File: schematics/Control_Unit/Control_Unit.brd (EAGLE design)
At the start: 49.8 x 49.8 mm, 274 parts, among them IC1 74HC174N, IC10 74HC74N, IC101 74HCT08N, IC102 74HC151N, IC103 74HC373N, IC105 74HC151N, IC106 74HC151N, IC108 74HCT32N, IC11 74HC74N, IC110 74HCT32N, IC111 74HC151N, IC112 74HCT32N, IC113 74HC151N, IC114 74HC151N, IC115 74HC151N, IC116 74HC373N, IC117 74HC74N, IC12 74AC08N, IC124 74HCT32N, IC125 74HCT08N, IC126 74AC157N, IC127 74HCT08N, IC128 74AC08N, IC129 74AC08N, IC13 74AC08N, IC134 74HCT08N, IC135 74HCT08N, IC136 74HCT08N, IC14 74HC74N, IC141 74HCT32N, IC15 74HC74N, IC16 74AC08N, IC168 74HCT32N, IC169 74HCT32N, IC17 74HCT32N, IC172 74HCT32N, IC173 74HCT32N, IC175 74HC193N, IC176 74HC193N, IC177 74HC193N, IC178 74HC193N, IC179 74HC193N, IC18 74AC08N, IC180 74HC193N, IC181 74HC193N, IC182 74HC193N, IC19 74AC08N, IC190 74HCT32N, IC191 74HCT32N, IC2 74HC174N, IC20 74AC08N, IC21 74AC08N, IC22 74HCT32N, IC23 74HCT08N, IC24 74HCT08N, IC25 74HCT32N, IC26 74HCT08N, IC27 74HCT08N, IC28 74HCT08N, IC29 74HCT32N, IC3 74HC151N, IC30 74HCT08N, IC31 74HCT00N, IC32 74HCT32N, IC33 74HCT32N, IC34 74HCT08N, IC35 74HCT04N, IC36 74HCT32N, IC37 74ACT02N, IC38 74HCT08N, IC39 74HCT08N, IC4 74HC174N, IC40 74HCT08N, IC41 74HCT08N, IC42 74HC373N, IC43 74HCT04N, IC44 74ACT157N, IC45 74HC373N, IC46 74ACT157N, IC47 74HCT04N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

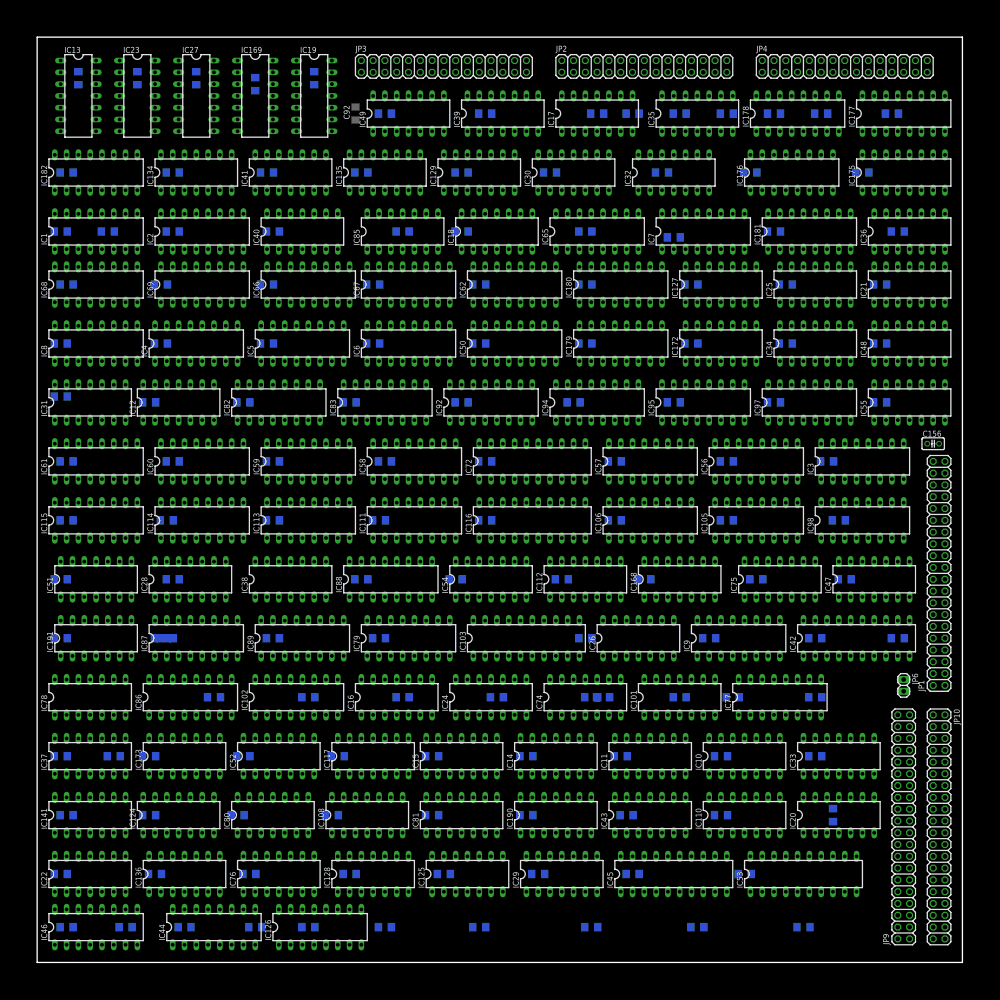
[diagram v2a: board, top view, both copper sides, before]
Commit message: changed register chips to 74xx374
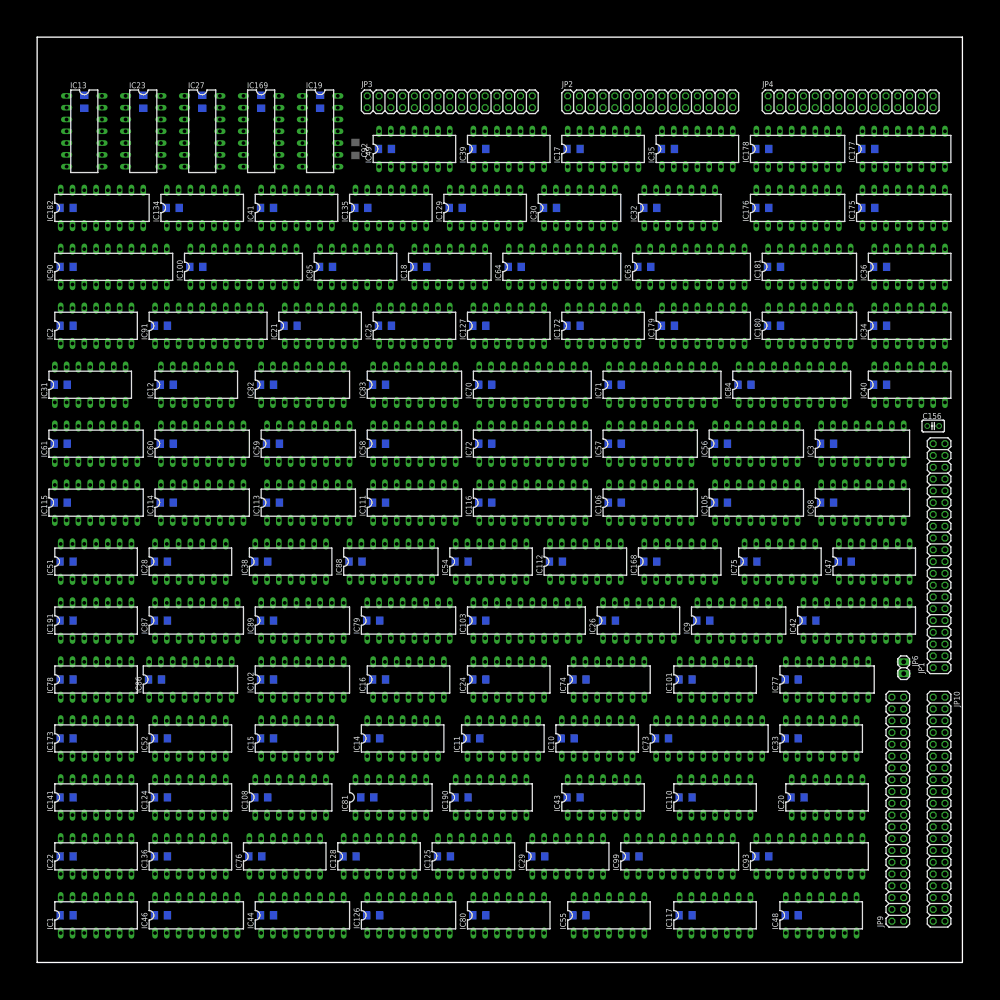
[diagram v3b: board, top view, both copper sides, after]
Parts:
- removed C102, C103, C104, C105, C106, C107, C108, C109, C133, C134, C135, C136, C137, C138, C139, C140, C152, C45, C94, C95, C98: (no value), rcl:C1206
- removed IC37: 74ACT02N, 74xx-eu:DIL14
- removed IC4, IC5, IC50, IC6, IC62, IC65, IC66, IC67, IC68, IC69, IC7, IC8, IC92, IC94, IC95, IC97: 74HC174N, 74xx-eu:DIL16
- removed IC45, IC53: 74HC373N, 74xx-eu:DIL20
- added IC100, IC63, IC64, IC70, IC71, IC73, IC84, IC90, IC91, IC93, IC99: 74HCT374N, 74xx-eu:DIL20
- IC1, IC2: value 74HC174N -> 74HCT32N; device 74xx-eu:DIL16 -> 74xx-eu:DIL14
- moved C90 51.2 mm to (1.59, 8.89)
- moved C22 40.5 mm to (22.9, 8.89), turned to 180 degrees
- moved C121 37.9 mm to (40.6, 2.54)
- moved IC1 36.8 mm to (3.17, 2.54)
- moved C132 34.9 mm to (36.8, 27.9)
- moved C13 34.5 mm to (12.1, 21.6)
- moved IC40 33.7 mm to (47.0, 31.1)
- moved C48 32.2 mm to (28.9, 8.89), turned to 180 degrees
- moved IC55 32.0 mm to (30.8, 2.54)
- moved IC21 31.8 mm to (15.2, 34.3)
- moved C44 31.7 mm to (33.0, 40.6)
- moved IC48 31.2 mm to (42.2, 2.54)
- moved C114 27.1 mm to (33.7, 12.1)
- moved C77 26.8 mm to (13.7, 34.3)
- moved C67 24.9 mm to (23.8, 18.4)
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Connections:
- net !REGISTER_RESET: no longer IC1.1, IC2.1, IC2.11, IC2.13, IC2.14, IC2.6, IC4.1, IC5.1, IC5.11, IC5.13, IC5.14, IC5.6, IC50.1, IC50.11, IC50.13, IC50.14, IC50.6, IC6.1, IC62.1, IC65.1, IC65.11, IC65.13, IC65.14, IC65.6, IC66.1, IC67.1, IC67.11, IC67.13, IC67.14, IC67.6, IC68.1, IC69.1, IC69.11, IC69.13, IC69.14, IC69.6, IC7.1, IC8.1, IC8.11, IC8.13, IC8.14, IC8.6, IC92.1, IC94.1, IC94.11, IC94.13, IC94.14, IC94.6, IC95.1, IC97.1, IC97.11, IC97.13, IC97.14, IC97.6
- net DATA0: now also IC100.3, IC63.3, IC64.3, IC70.3, IC71.3, IC73.3, IC84.3, IC90.3, IC91.3, IC93.3, IC99.3; no longer IC1.3, IC4.3, IC45.3, IC53.3, IC6.3, IC62.3, IC66.3, IC68.3, IC7.3, IC92.3, IC95.3
- net DATA1: now also IC100.4, IC63.4, IC64.4, IC70.4, IC71.4, IC73.4, IC84.4, IC90.4, IC91.4, IC93.4, IC99.4; no longer IC1.4, IC4.4, IC45.4, IC53.4, IC6.4, IC62.4, IC66.4, IC68.4, IC7.4, IC92.4, IC95.4
- net DATA2: now also IC100.7, IC63.7, IC64.7, IC70.7, IC71.7, IC73.7, IC84.7, IC90.7, IC91.7, IC93.7, IC99.7; no longer IC1.6, IC4.6, IC45.7, IC53.7, IC6.6, IC62.6, IC66.6, IC68.6, IC7.6, IC92.6, IC95.6
- net DATA3: now also IC100.8, IC63.8, IC64.8, IC70.8, IC71.8, IC73.8, IC84.8, IC90.8, IC91.8, IC93.8, IC99.8; no longer IC1.11, IC4.11, IC45.8, IC53.8, IC6.11, IC62.11, IC66.11, IC68.11, IC7.11, IC92.11, IC95.11
- net DATA4: now also IC100.13, IC63.13, IC64.13, IC70.13, IC71.13, IC73.13, IC84.13, IC90.13, IC91.13, IC93.13, IC99.13; no longer IC1.13, IC4.13, IC45.13, IC53.13, IC6.13, IC62.13, IC66.13, IC68.13, IC7.13, IC92.13, IC95.13
- net DATA5: now also IC100.14, IC63.14, IC70.14, IC71.14, IC73.14, IC84.14, IC90.14, IC91.14, IC93.14, IC99.14; no longer IC1.14, IC4.14, IC45.14, IC6.14, IC62.14, IC66.14, IC68.14, IC7.14, IC92.14, IC95.14
- net DATA6: now also IC100.17, IC63.17, IC64.14, IC64.17, IC70.17, IC71.17, IC73.17, IC84.17, IC90.17, IC91.17, IC93.17, IC99.17; no longer IC2.3, IC45.17, IC5.3, IC50.3, IC53.14, IC53.17, IC65.3, IC67.3, IC69.3, IC8.3, IC94.3, IC97.3
- net DATA7: now also IC100.18, IC63.18, IC64.18, IC70.18, IC71.18, IC73.18, IC84.18, IC90.18, IC91.18, IC93.18, IC99.18; no longer IC2.4, IC45.18, IC5.4, IC50.4, IC53.18, IC65.4, IC67.4, IC69.4, IC8.4, IC94.4, IC97.4
- net FILL_LR_H_SAVE_LR: now also IC2.12; no longer IC37.11
- net FILL_LR_L_SAVE_LR: now also IC1.4; no longer IC37.5
- net FILL_PTR_H_SET_PTR: now also IC2.5; no longer IC37.3
- net FILL_PTR_L_SET_PTR: now also IC2.2; no longer IC37.9
- net GND: now also IC1.7, IC100.1, IC100.10, IC2.7, IC63.1, IC63.10, IC64.1, IC64.10, IC70.1, IC70.10, IC71.1, IC71.10, IC73.1, IC73.10, IC84.1, IC84.10, IC90.1, IC90.10, IC91.1, IC91.10, IC93.1, IC93.10, IC99.1, IC99.10; no longer C102.2, C103.2, C104.2, C105.2, C106.2, C107.2, C108.2, C109.2, C133.2, C134.2, C135.2, C136.2, C137.2, C138.2, C139.2, C140.2, C152.2, C45.2, C94.2, C95.2, C98.2, IC1.8, IC2.8, IC37.7, IC4.8, IC45.1, IC45.10, IC5.8, IC50.8, IC53.1, IC53.10, IC6.8, IC62.8, IC65.8, IC66.8, IC67.8, IC68.8, IC69.8, IC7.8, IC8.8, IC92.8, IC94.8, IC95.8, IC97.8
- net IO_OUTPUT1_0: now also IC63.2; no longer IC45.2
- net IO_OUTPUT1_1: now also IC63.5; no longer IC45.5
- net IO_OUTPUT1_2: now also IC63.6; no longer IC45.6
- net IO_OUTPUT1_3: now also IC63.9; no longer IC45.9
- net IO_OUTPUT1_4: now also IC63.12; no longer IC45.12
- net IO_OUTPUT1_5: now also IC63.15; no longer IC45.15
- net IO_OUTPUT1_6: now also IC63.16; no longer IC45.16
- net IO_OUTPUT1_7: now also IC63.19; no longer IC45.19
- net IO_OUTPUT2_0: now also IC64.2; no longer IC53.2
- net IO_OUTPUT2_1: now also IC64.5; no longer IC53.5
- net IO_OUTPUT2_2: now also IC64.6; no longer IC53.6
- net IO_OUTPUT2_3: now also IC64.9; no longer IC53.9
- net IO_OUTPUT2_4: now also IC64.12; no longer IC53.12
- net IO_OUTPUT2_5: now also IC64.15; no longer IC53.15
- net IO_OUTPUT2_6: now also IC64.16; no longer IC53.16
- net IO_OUTPUT2_7: now also IC64.19; no longer IC53.19
- net IO_OUTPUT_REG_1_LOAD_INPUT: now also IC63.11; no longer IC45.11
- net IO_OUTPUT_REG_2_LOAD_INPUT: now also IC64.11; no longer IC53.11
- net IR_DATA_OUT_0: now also IC90.2; no longer IC4.2
- net IR_DATA_OUT_1: now also IC90.5; no longer IC4.5
- net IR_DATA_OUT_2: now also IC90.6; no longer IC4.7
- net IR_DATA_OUT_3: now also IC90.9; no longer IC4.10
- net IR_DATA_OUT_4: now also IC90.12; no longer IC4.12
- net IR_DATA_OUT_5: now also IC90.15; no longer IC4.15
- net IR_DATA_OUT_6: now also IC90.16; no longer IC5.2
- net IR_DATA_OUT_7: now also IC90.19; no longer IC5.5
- net IR_LOAD_INPUT: now also IC90.11; no longer IC4.9, IC5.9
- net LR_DATA_OUT_0: now also IC99.2; no longer IC92.2
- net LR_DATA_OUT_1: now also IC99.5; no longer IC92.5
- net LR_DATA_OUT_10: now also IC100.6; no longer IC95.7
- net LR_DATA_OUT_11: now also IC100.9; no longer IC95.10
- net LR_DATA_OUT_12: now also IC100.12; no longer IC95.12
- net LR_DATA_OUT_13: now also IC100.15; no longer IC95.15
- net LR_DATA_OUT_14: now also IC100.16; no longer IC97.2
- net LR_DATA_OUT_15: now also IC100.19; no longer IC97.5
- net LR_DATA_OUT_2: now also IC99.6; no longer IC92.7
- net LR_DATA_OUT_3: now also IC99.9; no longer IC92.10
- net LR_DATA_OUT_4: now also IC99.12; no longer IC92.12
- net LR_DATA_OUT_5: now also IC99.15; no longer IC92.15
- net LR_DATA_OUT_6: now also IC99.16; no longer IC94.2
- net LR_DATA_OUT_7: now also IC99.19; no longer IC94.5
- net LR_DATA_OUT_8: now also IC100.2; no longer IC95.2
- net LR_DATA_OUT_9: now also IC100.5; no longer IC95.5
- net LR_H_LOAD_INPUT_NOT: now also IC100.11, IC2.11; no longer IC37.13, IC95.9, IC97.9
- net LR_H_LOAD_INPUT_TABLE_1: now also IC2.13; no longer IC37.12
- net LR_L_LOAD_INPUT_NOT: now also IC1.6, IC99.11; no longer IC37.4, IC92.9, IC94.9
- net LR_L_LOAD_INPUT_TABLE_1: now also IC1.5; no longer IC37.6
- net OPCODE_0: now also IC91.2; no longer IC6.2
- net OPCODE_1: now also IC91.5; no longer IC6.5
- net OPCODE_2: now also IC91.6; no longer IC6.7
- net OPCODE_3: now also IC91.9; no longer IC6.10
- net OPCODE_4: now also IC91.12; no longer IC6.12
- net OPCODE_5: now also IC91.15; no longer IC6.15
- net OPCODE_6: now also IC91.16; no longer IC50.2
- net OPCODE_7: now also IC91.19; no longer IC50.5
- net OPCODE_LOAD_INPUT/CYCL_2: now also IC91.11; no longer IC50.9, IC6.9
- net PC_COUNT_UP: now also IC2.8; no longer IC54.4
- net PC_COUNT_UP_FETCH1: now also IC2.9; no longer IC54.5
- net PC_COUNT_UP_FETCH2/CYCL_5: now also IC2.10; no longer IC54.6
- net PTR_DATA_OUT_0: now also IC93.2; no longer IC1.2
- net PTR_DATA_OUT_1: now also IC93.5; no longer IC1.5
- net PTR_DATA_OUT_2: now also IC93.6; no longer IC1.7
- net PTR_DATA_OUT_3: now also IC93.9; no longer IC1.10
- net PTR_DATA_OUT_4: now also IC93.12; no longer IC1.12
- net PTR_DATA_OUT_5: now also IC93.15; no longer IC1.15
- net PTR_DATA_OUT_6: now also IC93.16; no longer IC2.2
- net PTR_DATA_OUT_7: now also IC93.19; no longer IC2.5
- net PTR_H_LOAD_INPUT_NOT: now also IC2.6; no longer IC37.1
- net PTR_L_LOAD_INPUT_NOT: now also IC2.3, IC93.11; no longer IC1.9, IC2.9, IC37.10
- net REG_0_LOAD_INPUT: now also IC84.11; no longer IC7.9, IC8.9
- net REG_0_OUT_0: now also IC84.2; no longer IC7.2
- net REG_0_OUT_1: now also IC84.5; no longer IC7.5
- net REG_0_OUT_2: now also IC84.6; no longer IC7.7
- net REG_0_OUT_3: now also IC84.9; no longer IC7.10
- net REG_0_OUT_4: now also IC84.12; no longer IC7.12
- net REG_0_OUT_5: now also IC84.15; no longer IC7.15
- net REG_0_OUT_6: now also IC84.16; no longer IC8.2
- net REG_0_OUT_7: now also IC84.19; no longer IC8.5
- net REG_1_LOAD_INPUT: now also IC70.11; no longer IC62.9, IC65.9
- net REG_1_OUT_0: now also IC70.2; no longer IC62.2
- net REG_1_OUT_1: now also IC70.5; no longer IC62.5
- net REG_1_OUT_2: now also IC70.6; no longer IC62.7
- net REG_1_OUT_3: now also IC70.9; no longer IC62.10
- net REG_1_OUT_4: now also IC70.12; no longer IC62.12
- net REG_1_OUT_5: now also IC70.15; no longer IC62.15
- net REG_1_OUT_6: now also IC70.16; no longer IC65.2
- net REG_1_OUT_7: now also IC70.19; no longer IC65.5
- net REG_2_LOAD_INPUT: now also IC73.11; no longer IC66.9, IC67.9
- net REG_2_OUT_0: now also IC73.2; no longer IC66.2
- net REG_2_OUT_1: now also IC73.5; no longer IC66.5
- net REG_2_OUT_2: now also IC73.6; no longer IC66.7
- net REG_2_OUT_3: now also IC73.9; no longer IC66.10
- net REG_2_OUT_4: now also IC73.12; no longer IC66.12
- net REG_2_OUT_5: now also IC73.15; no longer IC66.15
- net REG_2_OUT_6: now also IC73.16; no longer IC67.2
- net REG_2_OUT_7: now also IC73.19; no longer IC67.5
- net REG_3_LOAD_INPUT: now also IC71.11; no longer IC68.9, IC69.9
- net REG_3_OUT_0: now also IC71.2; no longer IC68.2
- net REG_3_OUT_1: now also IC71.5; no longer IC68.5
- net REG_3_OUT_2: now also IC71.6; no longer IC68.7
- net REG_3_OUT_3: now also IC71.9; no longer IC68.10
- net REG_3_OUT_4: now also IC71.12; no longer IC68.12
- net REG_3_OUT_5: now also IC71.15; no longer IC68.15
- net REG_3_OUT_6: now also IC71.16; no longer IC69.2
- net REG_3_OUT_7: now also IC71.19; no longer IC69.5
- net TABLE_1_INPUT_PTR_HIGH: now also IC2.4; no longer IC37.2
- net TABLE_1_INPUT_PTR_L: now also IC2.1; no longer IC37.8
- net VCC: now also IC1.14, IC100.20, IC2.14, IC63.20, IC64.20, IC70.20, IC71.20, IC73.20, IC84.20, IC90.20, IC91.20, IC93.20, IC99.20; no longer C102.1, C103.1, C104.1, C105.1, C106.1, C107.1, C108.1, C109.1, C133.1, C134.1, C135.1, C136.1, C137.1, C138.1, C139.1, C140.1, C152.1, C45.1, C94.1, C95.1, C98.1, IC1.16, IC2.16, IC37.14, IC4.16, IC45.20, IC5.16, IC50.16, IC53.20, IC6.16, IC62.16, IC65.16, IC66.16, IC67.16, IC68.16, IC69.16, IC7.16, IC8.16, IC92.16, IC94.16, IC95.16, IC97.16

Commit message: forgot it
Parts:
- removed C156: (no value), rcl:C025-025X050
- moved IC79 17.5 mm to (37.5, 18.4)
- moved IC101 16.8 mm to (20.0, 18.4)
- moved IC103 15.6 mm to (41.6, 15.2)
- moved C67 11.7 mm to (35.6, 18.4)
- moved IC77 7.30 mm to (35.2, 15.2)
- moved C35 6.67 mm to (24.1, 18.4)
- moved C61 6.67 mm to (29.2, 18.4)
- moved IC26 6.67 mm to (25.7, 18.4)
- moved IC9 6.35 mm to (31.4, 18.4)
- moved C150 1.59 mm to (33.3, 15.2)
- moved C122 1.27 mm to (8.89, 47.6)
- moved C18 1.27 mm to (44.8, 45.1)
- moved C23 1.27 mm to (28.9, 45.1)
- moved C26 1.27 mm to (39.1, 45.1)
- moved C49 1.27 mm to (2.54, 47.6)
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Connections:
- net ADRR_15: now also IC17.9; no longer IC25.9
- net FILL_PC_H_RET: now also IC1.1; no longer IC17.12
- net FILL_PC_L_JMP_O: now also IC1.12; no longer IC80.9
- net FILL_PC_L_RET: now also IC1.13; no longer IC80.10
- net GND: no longer C156.2
- net MEM_NOT_CE: now also IC17.10, IC17.13; no longer IC25.10, IC36.2
- net N$12: now also IC49.13; no longer IC49.12
- net N$163: now also IC1.11; no longer IC80.8
- net N$171: now also IC36.6; no longer IC17.8
- net N$31: now also IC17.11; no longer IC36.3
- net N$32: now also IC1.8; no longer IC36.6
- net N$33: now also IC1.3; no longer IC17.11
- net N$67: now also IC17.12; no longer IC36.1
- net N$70: now also IC17.8; no longer IC25.8
- net PC_H_LOAD_INPUT_TABLE_1: now also IC1.2; no longer IC17.13
- net PC_LOW_LOAD_INPUT_JMP: now also IC1.9; no longer IC36.4
- net PC_L_LOAD_INPUT_TABLE_1: now also IC1.10; no longer IC36.5
- net VCC: now also IC49.12; no longer C156.1, IC49.13
- net WRITE_LR_H_DBUS_RET: now also IC36.4; no longer IC17.9
- net WRITE_PC_L_DBUS_SAVE_LR: now also IC36.5; no longer IC17.10

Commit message: regroup
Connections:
- net CONNECT_PTR_TO_ABUS/CLR_NOT_OE_LDR: now also IC36.1; no longer IC25.4
- net CONNECT_PTR_TO_ABUS/CONNECT_REG_TO_DBUS/CLR_NOT_WE/SELECTOR_TABLE_2_STR: now also IC36.2; no longer IC25.5
- net N$190: now also IC80.10; no longer IC25.2
- net N$192: now also IC80.9; no longer IC25.1
- net N$193: now also IC80.8; no longer IC25.3
- net PTR_TO_ABUS/!PC_TO_ABUS: now also IC36.3; no longer IC25.6

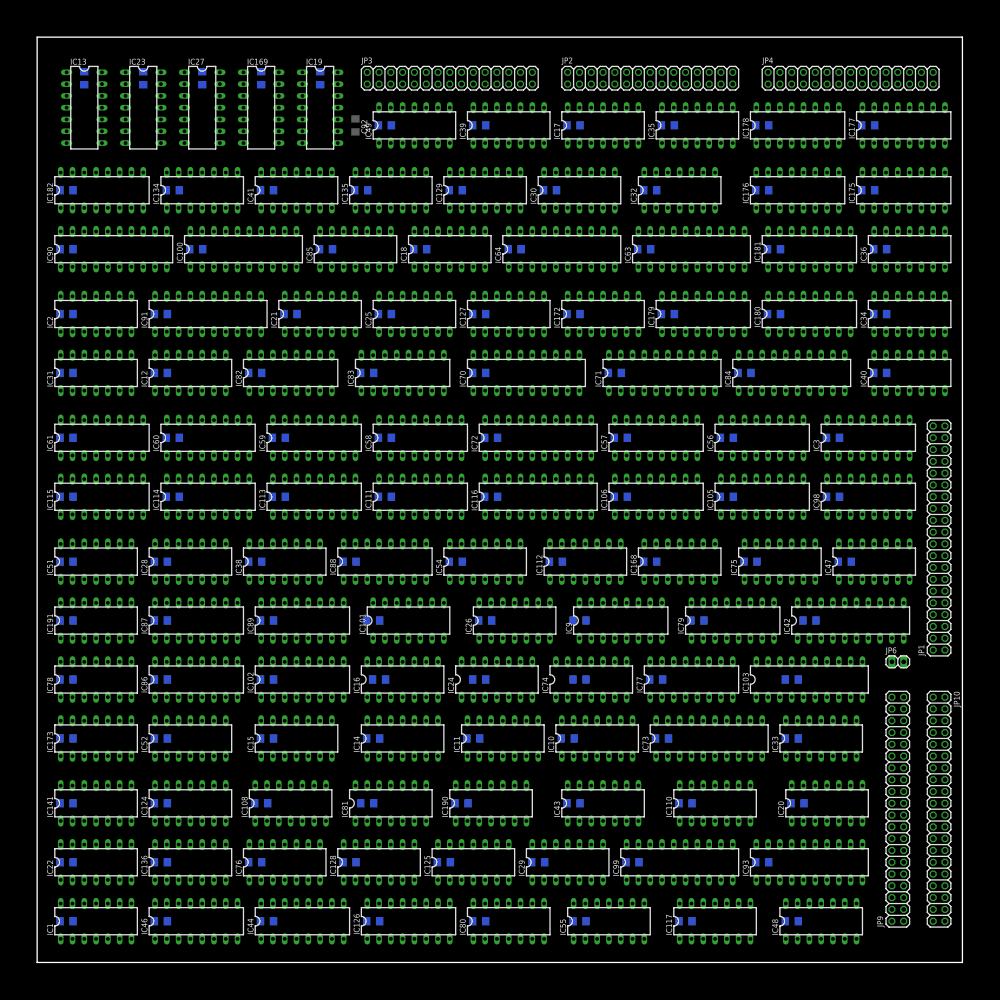
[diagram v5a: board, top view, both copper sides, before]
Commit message: optimize chip count :)
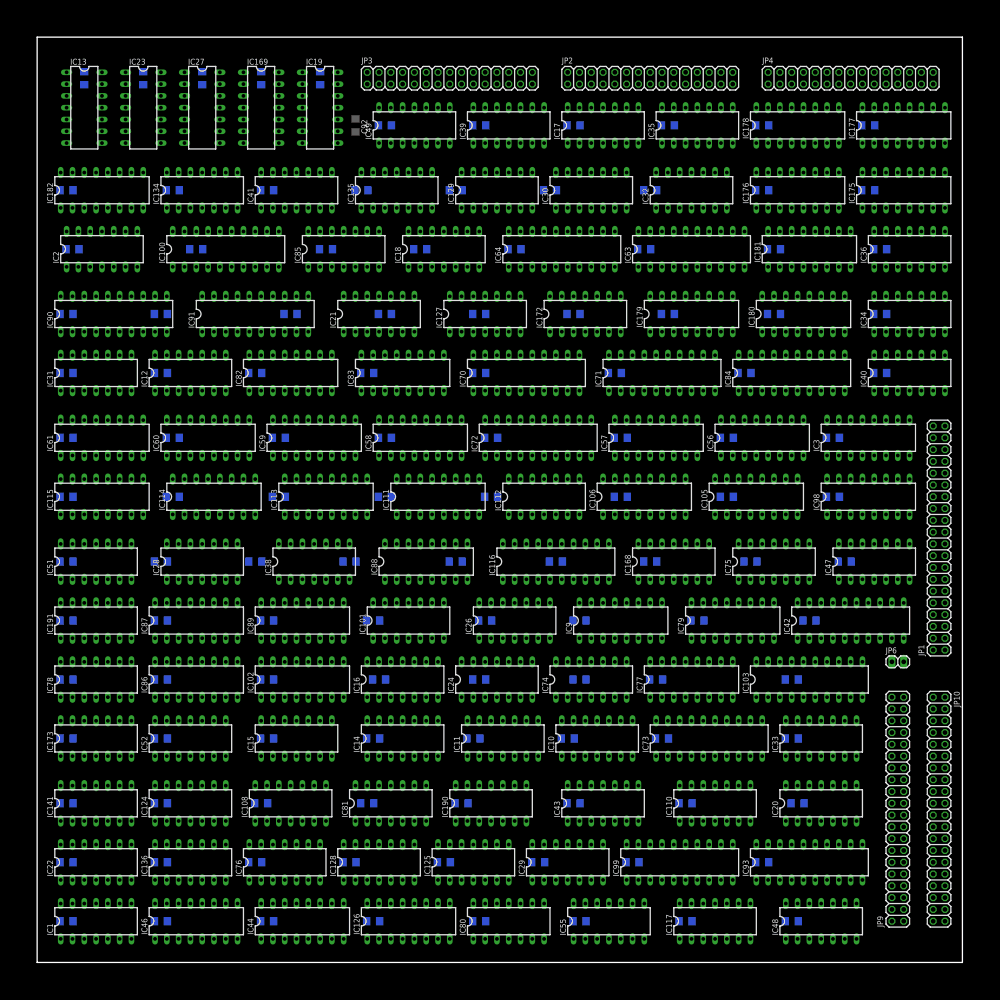
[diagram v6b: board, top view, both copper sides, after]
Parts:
- removed IC25: 74HCT32N, 74xx-eu:DIL14
- removed IC54: 74ACT02N, 74xx-eu:DIL14
- moved IC112 4.14 mm to (27.3, 25.1)
- moved IC116 3.62 mm to (27.9, 21.6)
- moved IC2 3.51 mm to (3.49, 38.4)
- moved IC90 3.49 mm to (4.13, 34.9)
- moved IC21 3.17 mm to (18.4, 34.9)
- moved IC91 2.54 mm to (11.7, 34.9)
- moved IC88 2.22 mm to (21.0, 21.6)
- moved IC38 1.59 mm to (14.9, 21.6)
- moved IC127 1.27 mm to (24.1, 34.9)
- moved IC100 0.95 mm to (10.2, 38.4)
- moved IC111 0.95 mm to (21.6, 25.1)
- moved IC172 0.95 mm to (29.5, 34.9)
- moved IC129 0.64 mm to (24.8, 41.6)
- moved IC113 0.63 mm to (15.6, 25.1)
- moved IC28 0.63 mm to (8.89, 21.6)
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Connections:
- removed net INPUT_REG0: IC126.3, IC129.3, IC135.1, IC135.4, IC30.1, IC31.4, IC41.1, IC41.4
- removed net N$201: IC54.13, IC80.1
- removed net N$217: IC108.11, IC48.11
- removed net N$224: IC136.12, IC136.2, IC34.6
- removed net N$227: IC169.5, IC48.13
- removed net N$247: IC136.10, IC136.13, IC43.8
- removed net N$54: IC34.4, IC43.10
- removed net N$84: IC128.6, IC76.5
- removed net N$85: IC128.8, IC76.10
- removed net N$86: IC128.11, IC76.13
- removed net OUTPUT_REG0_JMP: IC128.3, IC31.5, IC76.2
- new net INPUT_REG0/OPCODE_5/OPCODE_4_IS_NULL: IC126.3, IC129.3, IC135.1, IC135.4, IC30.1, IC34.1, IC40.5, IC41.1, IC41.4
- new net INPUT_REG_IS_OUTPUT_REG: IC40.9, IC43.10
- new net N$45: IC40.10, IC80.3
- new net OPC_67_OUPUT0/REG0_JMP: IC128.3, IC136.1, IC34.2, IC76.2
- new net OPC_67_OUPUT1: IC128.6, IC136.4, IC76.5
- new net OPC_67_OUPUT2: IC128.8, IC136.9, IC76.10
- new net OPC_67_OUPUT3: IC128.11, IC136.12, IC76.13
- net CLR_NOT_CS_POP: now also IC48.11; no longer IC54.2
- net CLR_NOT_OE_POP: now also IC48.13; no longer IC54.1
- net FILL_REGISTER_ALU/ALU_TO_DBUS: now also IC169.4; no longer IC54.8
- net GND: no longer IC25.7, IC54.7
- net INPUT_REG_IS_NOT_OUTPUT_REG: now also IC43.11; no longer IC48.12, IC54.11
- net N$12: now also IC40.11; no longer IC34.8
- net N$14: now also IC43.8; no longer IC54.10
- net N$147: now also IC169.5; no longer IC54.9
- net N$149: now also IC47.12; no longer IC31.6, IC47.13
- net N$157: now also IC48.12; no longer IC54.3
- net N$18: now also IC169.6, IC43.9; no longer IC136.5, IC136.9, IC34.3
- net N$185: now also IC108.13; no longer IC25.13
- net N$187: now also IC108.12; no longer IC25.12
- net N$20: now also IC108.11; no longer IC25.11
- net N$203: now also IC40.6; no longer IC169.6
- net N$206: now also IC80.1; no longer IC54.12
- net N$21: now also IC40.4; no longer IC169.4
- net N$22: now also IC34.3, IC47.13; no longer IC47.12
- net N$266: now also IC40.13; no longer IC34.10
- net N$53: now also IC136.10, IC136.13, IC136.2, IC136.5; no longer IC34.2, IC34.5
- net OPCODE_4: no longer IC108.12
- net OPCODE_5: no longer IC108.13
- net OPCODE_6: no longer IC34.1, IC43.11
- net OPCODE_7: no longer IC136.1, IC136.4, IC43.9
- net REGISTER_OUTPUT_SEL_3: now also IC40.12; no longer IC34.9
- net TWO_BYTE_CMD: now also IC40.8; no longer IC80.3
- net VCC: no longer IC25.14, IC54.14

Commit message: start routing
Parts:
- removed C115, C81, C92: (no value), rcl:C1206
- IC4: value 74HCT08N -> 74AC08N
- moved IC52 29.9 mm to (36.5, 2.22)
- moved IC117 29.6 mm to (8.63, 12.1)
- moved C77 4.45 mm to (9.21, 34.9)
- moved C112 2.22 mm to (19.1, 21.6)
- moved C32 2.22 mm to (25.7, 21.6)
- moved C116 1.91 mm to (16.8, 34.9)
- moved C13 1.59 mm to (13.3, 21.6)
- moved C1 1.59 mm to (39.1, 15.2)
- moved C14 1.27 mm to (7.30, 38.4)
- moved C29 1.27 mm to (25.7, 25.1)
- moved C56 1.27 mm to (22.5, 34.9)
- moved C154 0.95 mm to (28.3, 15.2)
- moved C130 0.95 mm to (14.6, 38.4)
- moved C33 0.95 mm to (27.9, 34.9)
- moved C80 0.95 mm to (19.7, 25.1)
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- renumbered IC76 to IC4
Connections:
- net OUTPUT_REG0 renamed N$72
- net OUTPUT_REG1 renamed N$69
- net OUTPUT_REG2 renamed N$27
- net OUTPUT_REG3 renamed N$24
- net GND: no longer C115.2, C81.2, C92.2
- net N$219: now also IC31.6; no longer IC34.11
- net N$44: now also IC31.4; no longer IC34.13
- net OPCODE_5: now also IC31.5; no longer IC35.11
- net SAVE_LR/RET: now also IC35.11; no longer IC34.12
- net VCC: no longer C115.1, C81.1, C92.1
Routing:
- net GND: track 0.00 -> 837.1 mm, vias 0 -> 2
- net VCC: track 0.00 -> 521.1 mm
- net RING_CNTR_CLOCK: track 0.00 -> 51.1 mm
